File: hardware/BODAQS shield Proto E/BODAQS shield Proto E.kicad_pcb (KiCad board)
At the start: 2 copper layers, 65 x 72.2 mm, 52 parts, among them J1 Analog Input 1, J3 Bar switch, J4 Navigation pad, J5 I2C Breakout, J6 Analog Input 2, J7 Analog Input 3, J8 Analog Input 4, J9 UART Breakout, U2 MCP6004, U4 LD1117V33

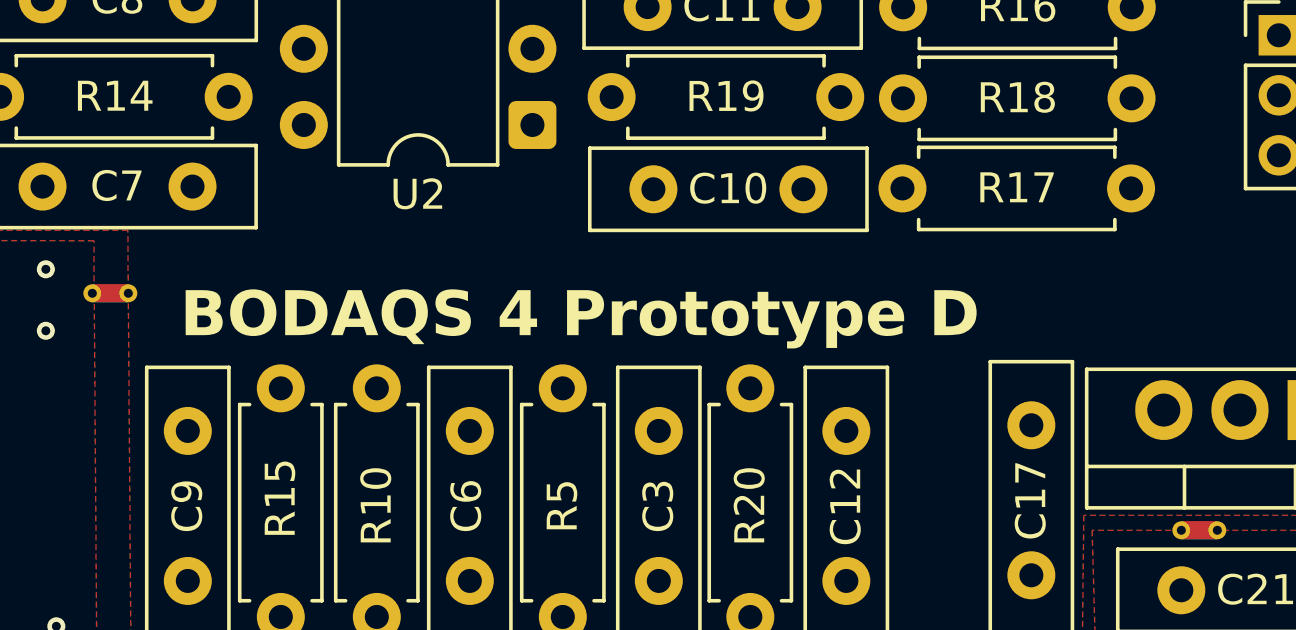
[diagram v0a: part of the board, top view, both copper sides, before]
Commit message: Add a test harness notebook for developing event definitions
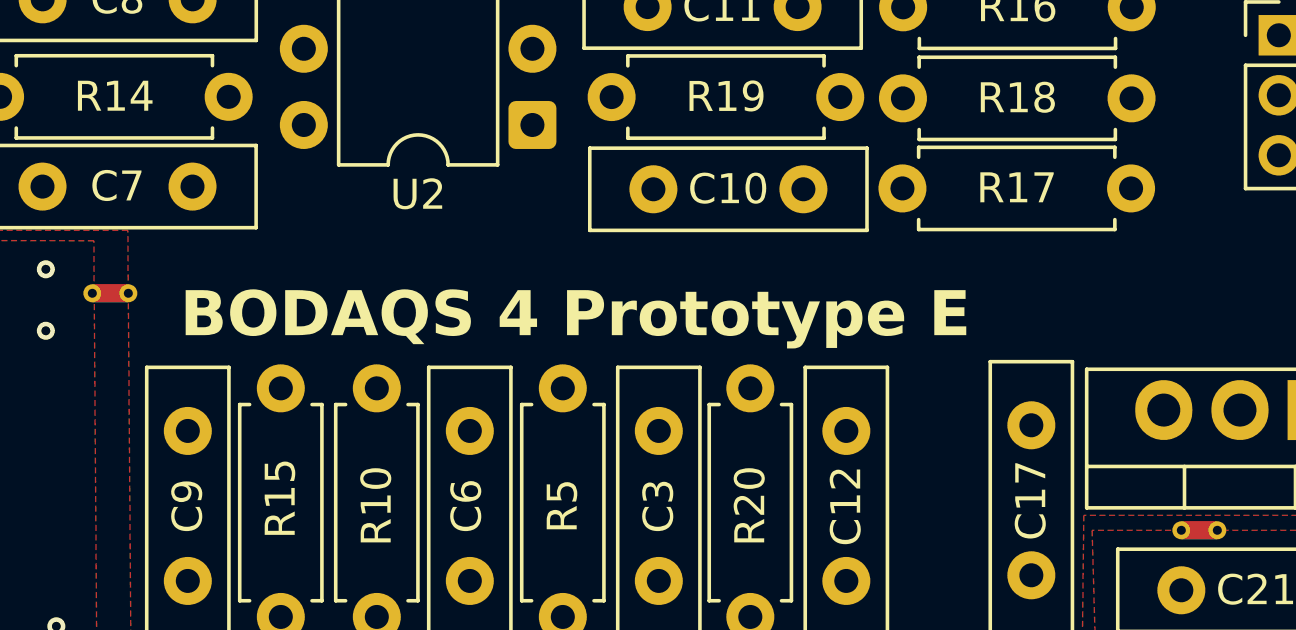
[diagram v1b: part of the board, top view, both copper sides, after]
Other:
- board text added: "BODAQS 4 Prototype E"
- board text removed: "BODAQS 4 Prototype D"
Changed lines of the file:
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@@
 		)
 	)
-	(gr_text "BODAQS 4 Prototype D"
+	(gr_text "BODAQS 4 Prototype E"
 		(at 161.621588 78.678752 0)
 		(layer "F.SilkS")

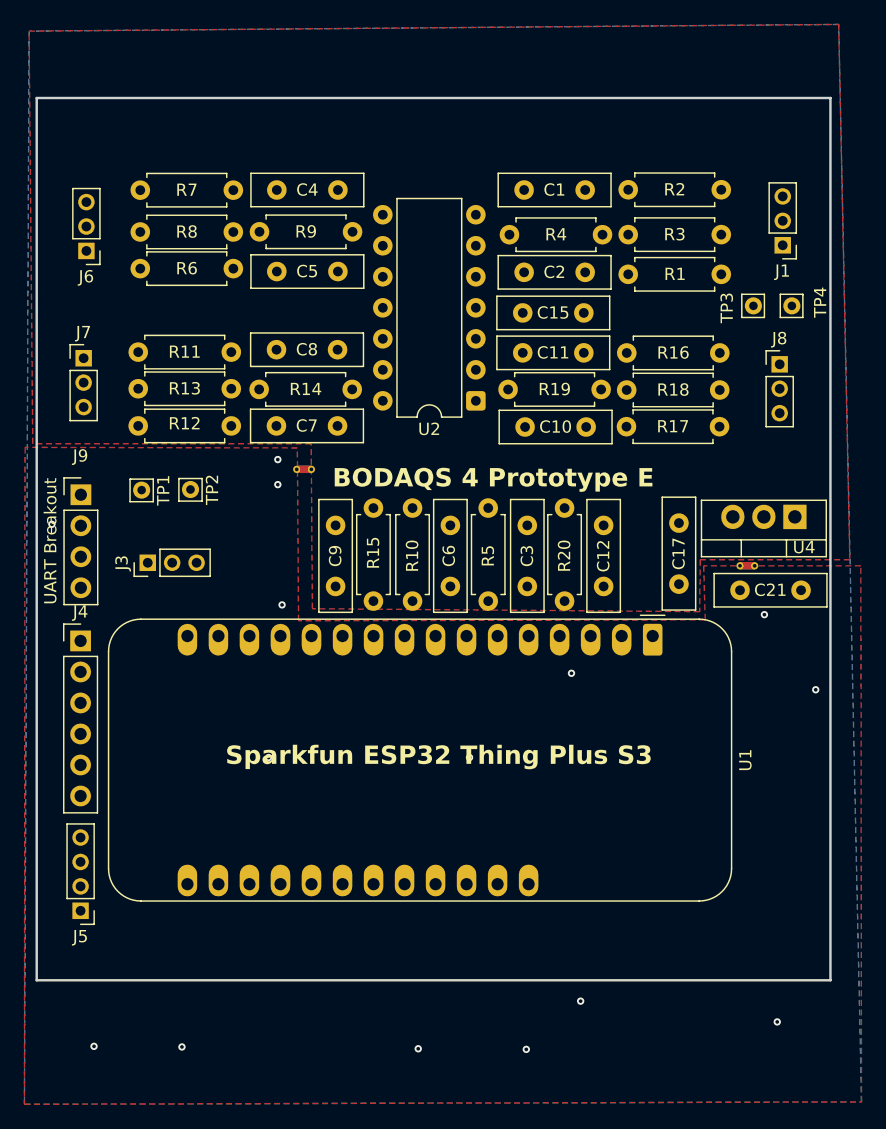
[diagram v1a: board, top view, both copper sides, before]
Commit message: Add shield prototype E designs; add test Sufni data
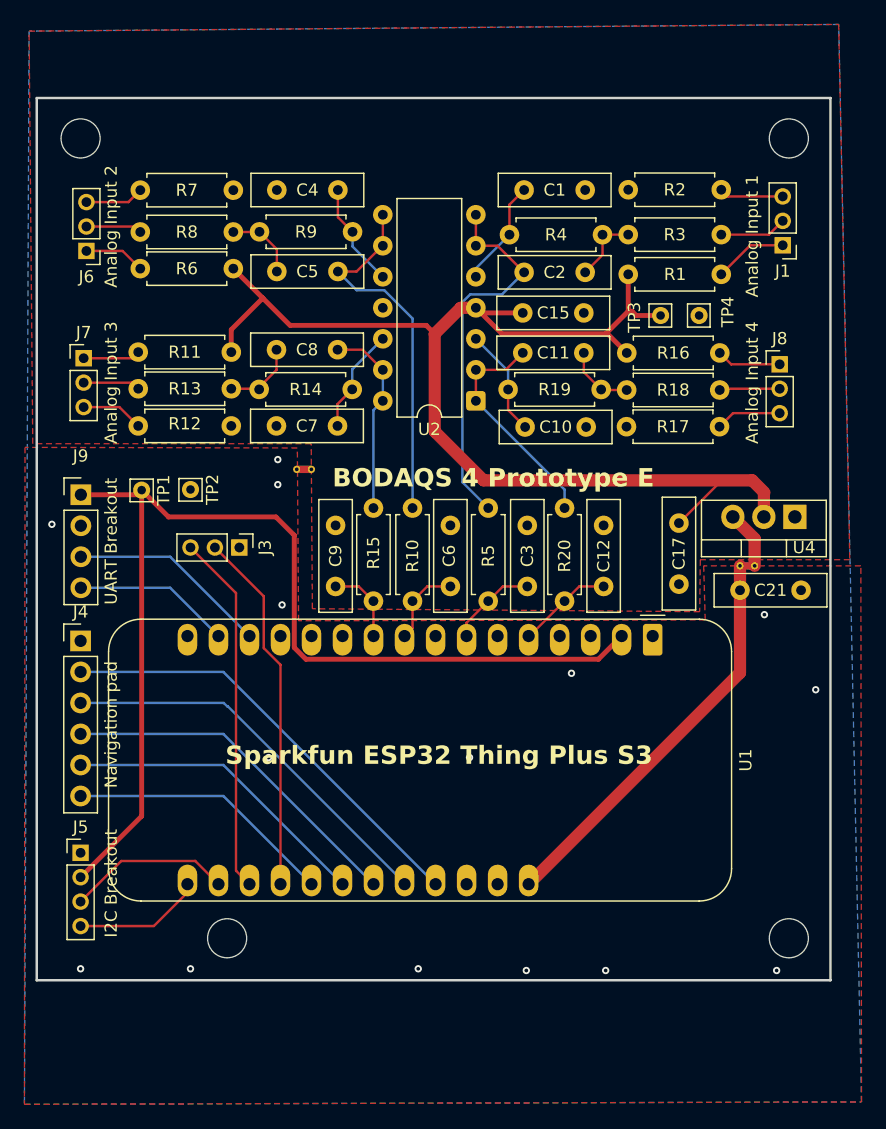
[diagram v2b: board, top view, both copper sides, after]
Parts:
- added REF**: MountingHole_3.2mm_M3, MountingHole:MountingHole_3.2mm_M3, F.Cu at (199.0, 115.5)
- added REF**: MountingHole_3.2mm_M3, MountingHole:MountingHole_3.2mm_M3, F.Cu at (199.0, 50.0)
- added REF**: MountingHole_3.2mm_M3, MountingHole:MountingHole_3.2mm_M3, F.Cu at (141.0, 50.0)
- added REF**: MountingHole_3.2mm_M3, MountingHole:MountingHole_3.2mm_M3, F.Cu at (153.0, 115.5)
- moved TP3 7.64 mm to (188.5, 64.5)
- moved TP4 7.64 mm to (191.7, 64.5)
- moved J3 7.60 mm to (154.0, 83.5), turned to -90 degrees
- moved J5 4.75 mm to (141.0, 108.5), turned to 0 degrees
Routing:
- net A3V3: track 0.00 -> 98.8 mm
- net +3V3: track 0.00 -> 90.1 mm
- net Enter: track 0.00 -> 36.3 mm
- net VBAT: track 0.00 -> 33.2 mm
- net Right: track 0.00 -> 32.7 mm
- net Net-(U2B--): track 0.00 -> 31.2 mm
- net Net-(U2C--): track 0.00 -> 30.3 mm
- net Mark: track 0.00 -> 29.8 mm
- net  LED: track 0.00 -> 29.6 mm
- net Left: track 0.00 -> 29.1 mm
- net Down: track 0.00 -> 25.5 mm
- net Up: track 0.00 -> 21.9 mm
- net Net-(U2A--): track 0.00 -> 18.7 mm
- net RXI: track 0.00 -> 16.5 mm
- net Net-(U2D--): track 0.00 -> 16.0 mm
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
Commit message: Finish hardware prototype E design (TH and SMD)
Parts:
- removed REF** (x4): MountingHole_3.2mm_M3, MountingHole:MountingHole_3.2mm_M3
- C1, C10, C4, C7: value 220nF -> 47nF
- C12, C3, C6, C9: value 100nF -> 10nF
- R13, R14, R18, R19, R3, R4, R8, R9: value 2K -> 4.7K
